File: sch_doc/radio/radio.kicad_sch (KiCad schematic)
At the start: 89 parts, among them IC1 MC34119, J1 tun, J2 out, J3 in_vol, J7 speaker, J8 vcc, J9 gnd, U1 ATTINY13A-PU, U2 TDA7088, U3 74HC595, U4 LM358

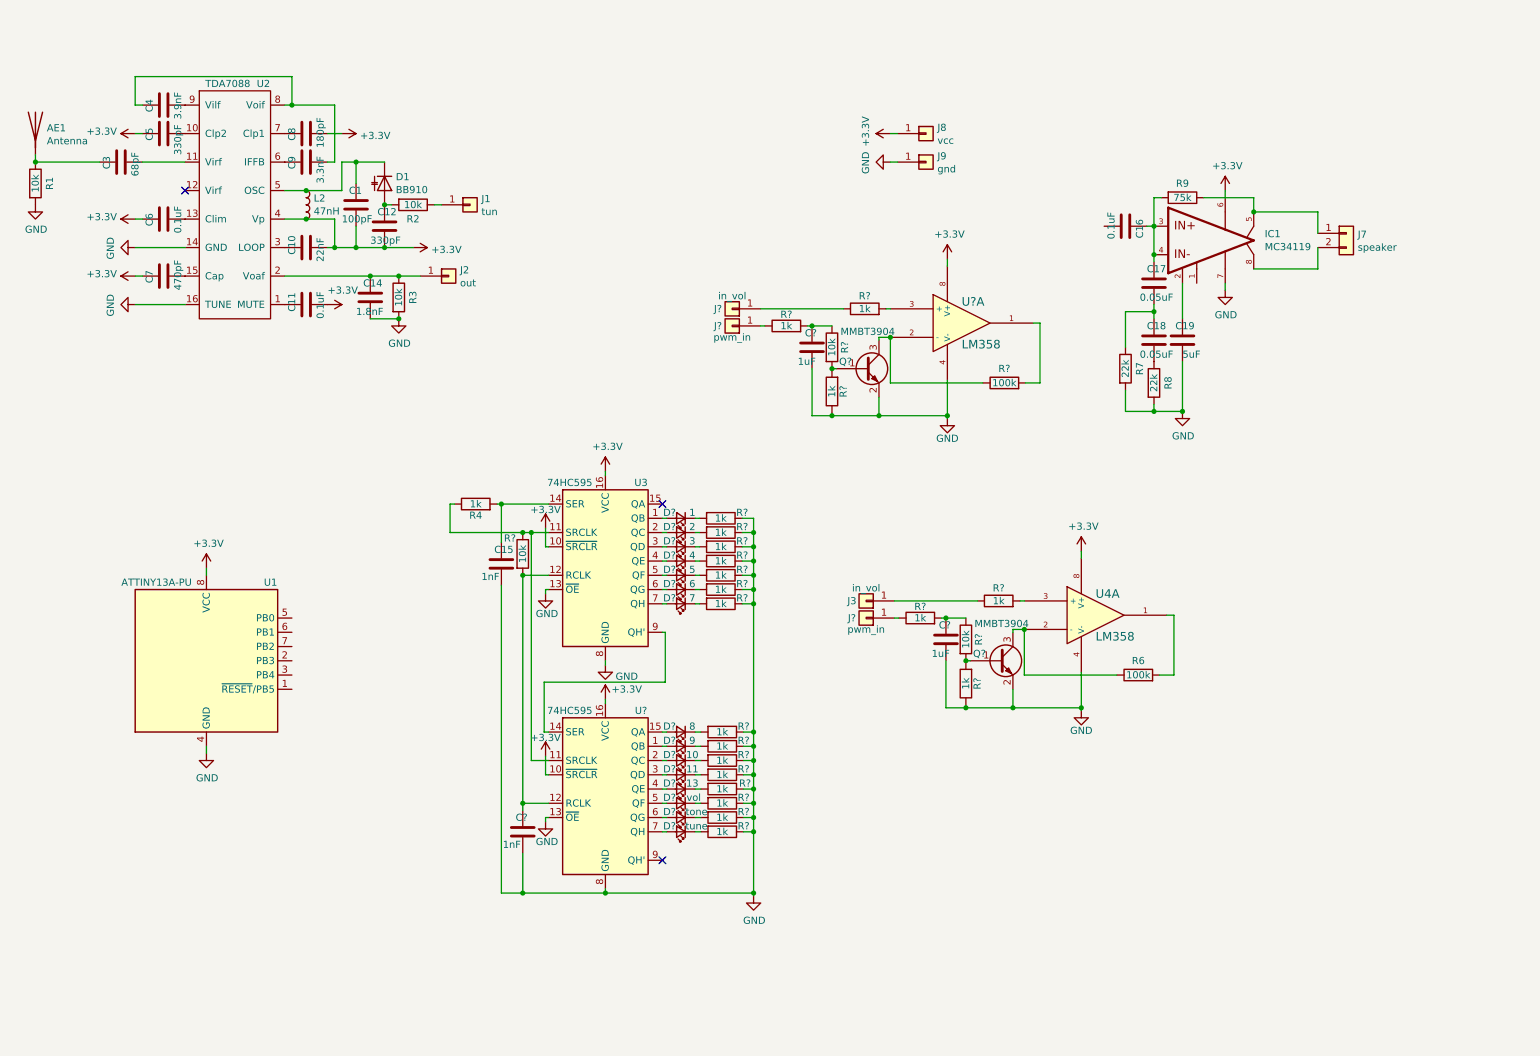
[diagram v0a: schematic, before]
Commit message: schematics ok, but not tested
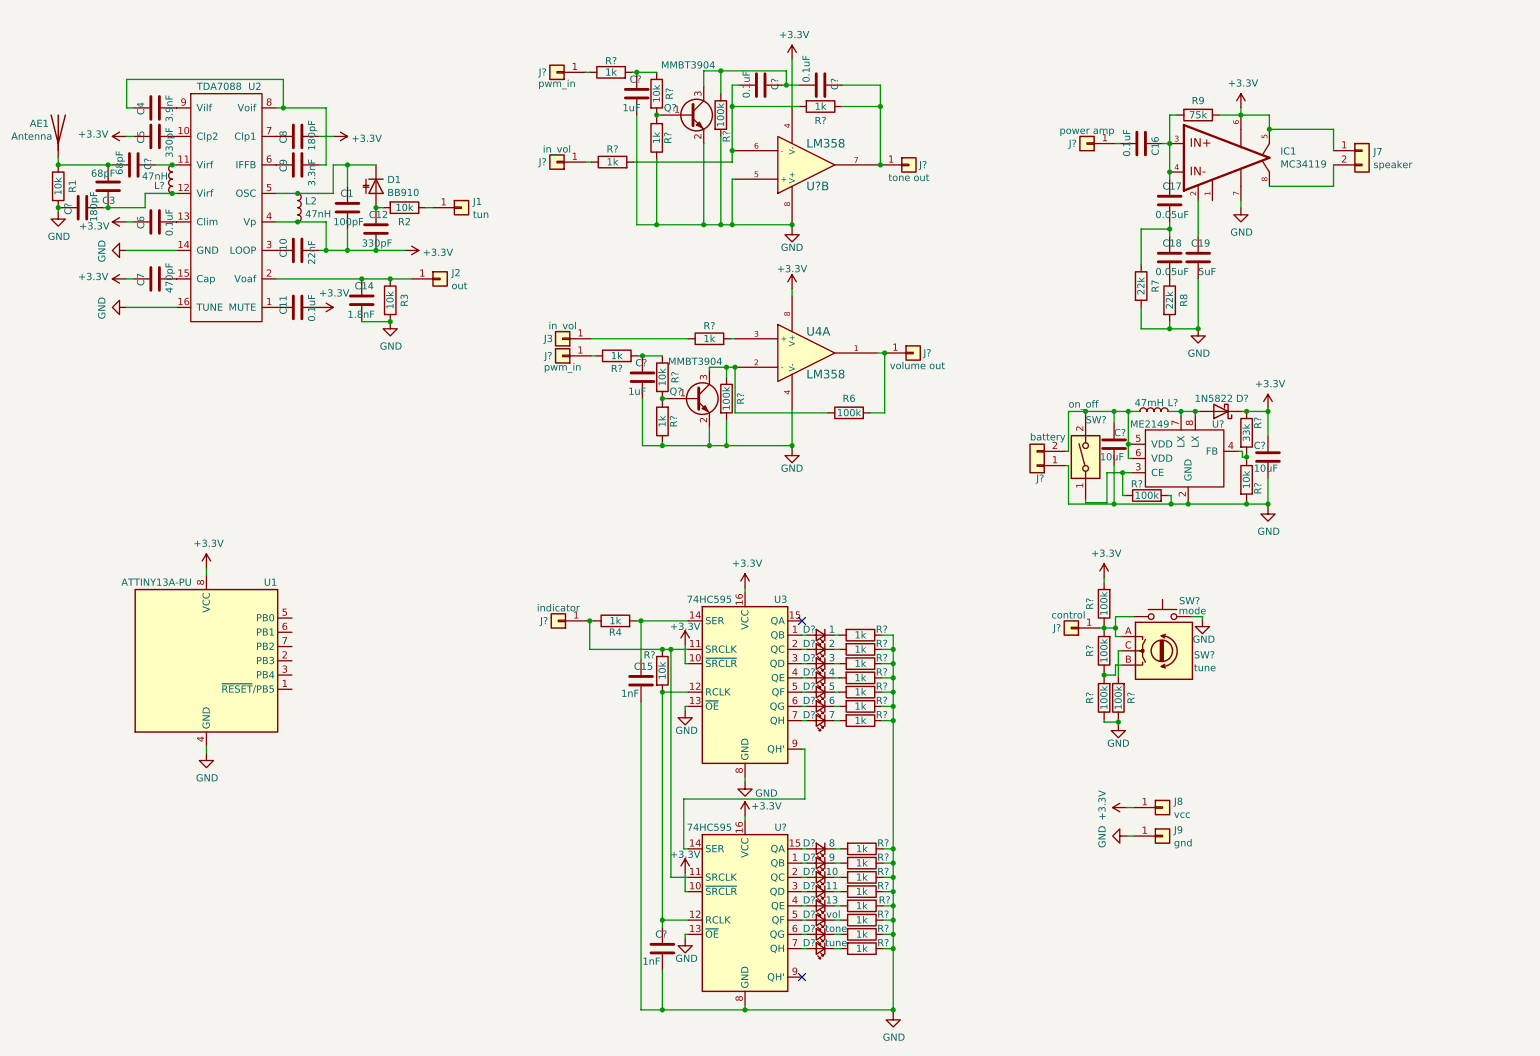
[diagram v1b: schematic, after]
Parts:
- removed C?: 1uF, Capacitor_SMD:C_0603_1608Metric, symbol Device:C
- removed Q?: MMBT3904, Package_TO_SOT_SMD:SOT-23, symbol Transistor_BJT:MMBT3904
- removed R? (x2): 1k, symbol Device:R
- removed R?: 10k, symbol Device:R
- added C?: 1uF, Capacitor_SMD:C_0603_1608Metric, symbol Device:C
- added C? (x2): 10uF, symbol Device:C
- added C? (x2): 0.1uF, symbol Device:C
- added C?: 68pF, Capacitor_SMD:C_0603_1608Metric, symbol Device:C
- added C?: 180pF, Capacitor_SMD:C_0603_1608Metric, symbol Device:C
- added D?: 1N5822, Diode_THT:D_DO-201AD_P15.24mm_Horizontal, symbol Diode:1N5822
- added J?: control, Connector_Wire:SolderWirePad_1x01_SMD_5x10mm, symbol Connector_Generic:Conn_01x01
- added J?: volume out, Connector_Wire:SolderWirePad_1x01_SMD_5x10mm, symbol Connector_Generic:Conn_01x01
- added J?: indicator, Connector_Wire:SolderWirePad_1x01_SMD_5x10mm, symbol Connector_Generic:Conn_01x01
- added J?: power amp, Connector_Wire:SolderWirePad_1x01_SMD_5x10mm, symbol Connector_Generic:Conn_01x01
- added J?: battery, symbol Connector_Generic:Conn_01x02
- added J?: tone out, Connector_Wire:SolderWirePad_1x01_SMD_5x10mm, symbol Connector_Generic:Conn_01x01
- added L?: 47mH, Inductor_SMD:L_0603_1608Metric_Pad1.05x0.95mm_HandSolder, symbol tda:L
- added L?: 47nH, Inductor_SMD:L_0603_1608Metric_Pad1.05x0.95mm_HandSolder, symbol tda:L
- added Q?: MMBT3904, Package_TO_SOT_SMD:SOT-23, symbol Transistor_BJT:MMBT3904
- added R? (x2): 1k, symbol Device:R
- added R? (x2): 10k, symbol Device:R
- added R?: 33k, symbol Device:R
- added R? (x6): 100k, Resistor_SMD:R_0805_2012Metric, symbol Device:R
- added R?: 100k, symbol Device:R
- added SW?: on_off, symbol Switch:SW_DIP_x01
- added SW?: mode, symbol Switch:SW_Push
- added SW?: tune, symbol Device:RotaryEncoder
- added U?: ME2149, symbol local:ME2149
- R?: value 100k -> 1k
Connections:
- net +3.3V: now also IC1.5, J7.1 (Pin_1), R9.1, U?.4 (V-), C?.2, D?.1 (K), R?.1, R?.2; no longer U?.8 (V+)
- net GND: now also U?.5 (+), U?.8 (V+), C?.1, C?.1, C?.1, C?.2, J?.1 (Pin_1), Q?.2 (E), R?.1, R?.1, R?.1, R?.2, R?.2, R?.2, R?.2, SW?.2, U?.2 (GND); no longer U?.4 (V-)
- net at C16.1: now also J?.1 (Pin_1)
- net at R4.1, R?.1, U3.11 (SRCLK)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: now also J?.1 (Pin_1)
- net at U2.11 (Virf): now also C?.2, L?.2; no longer C3.1
- net at U2.12 (Virf): now also C3.2, C?.1, L?.1
- net at R6.2, U4.1: now also J?.1 (Pin_1)
- net at Q?.3 (C), R6.1, U4.2 (-): now also R?.1
- net at AE1.1 (A), R1.1: now also C3.1, C?.1; no longer C3.2
- net at J?.1 (Pin_1): now also R?.1
- net at R?.2: now also R?.2, U?.6 (-), C?.1; no longer U?.1
- net at R?.1: now also U?.7, C?.2, J?.1 (Pin_1); no longer U?.2 (-)
- new net: C?.2, J?.2 (Pin_2), L?.1, SW?.2, U?.5 (VDD), U?.6 (VDD)
- new net: D?.2 (A), L?.2, U?.7 (LX), U?.8 (LX)
- new net: J?.1 (Pin_1), R?.1, R?.2, SW?.1, SW?.A
- new net: C?.2, R?.1, R?.2
- new net: Q?.1 (B), R?.2, R?.2
- new net: R?.1, SW?.1, U?.3 (CE)
- new net: C?.1, C?.2, Q?.3 (C), R?.1
- new net: R?.1, R?.2, SW?.B
- new net: R?.2, SW?.C
- new net: R?.1, R?.2, U?.4 (FB)
- no-connect marks 3 -> 2
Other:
- moved on the sheet: AE1, C1, C10, C11, C12, C14, C15, C16, C17, C18, C19, C3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

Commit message: pt2313 library element
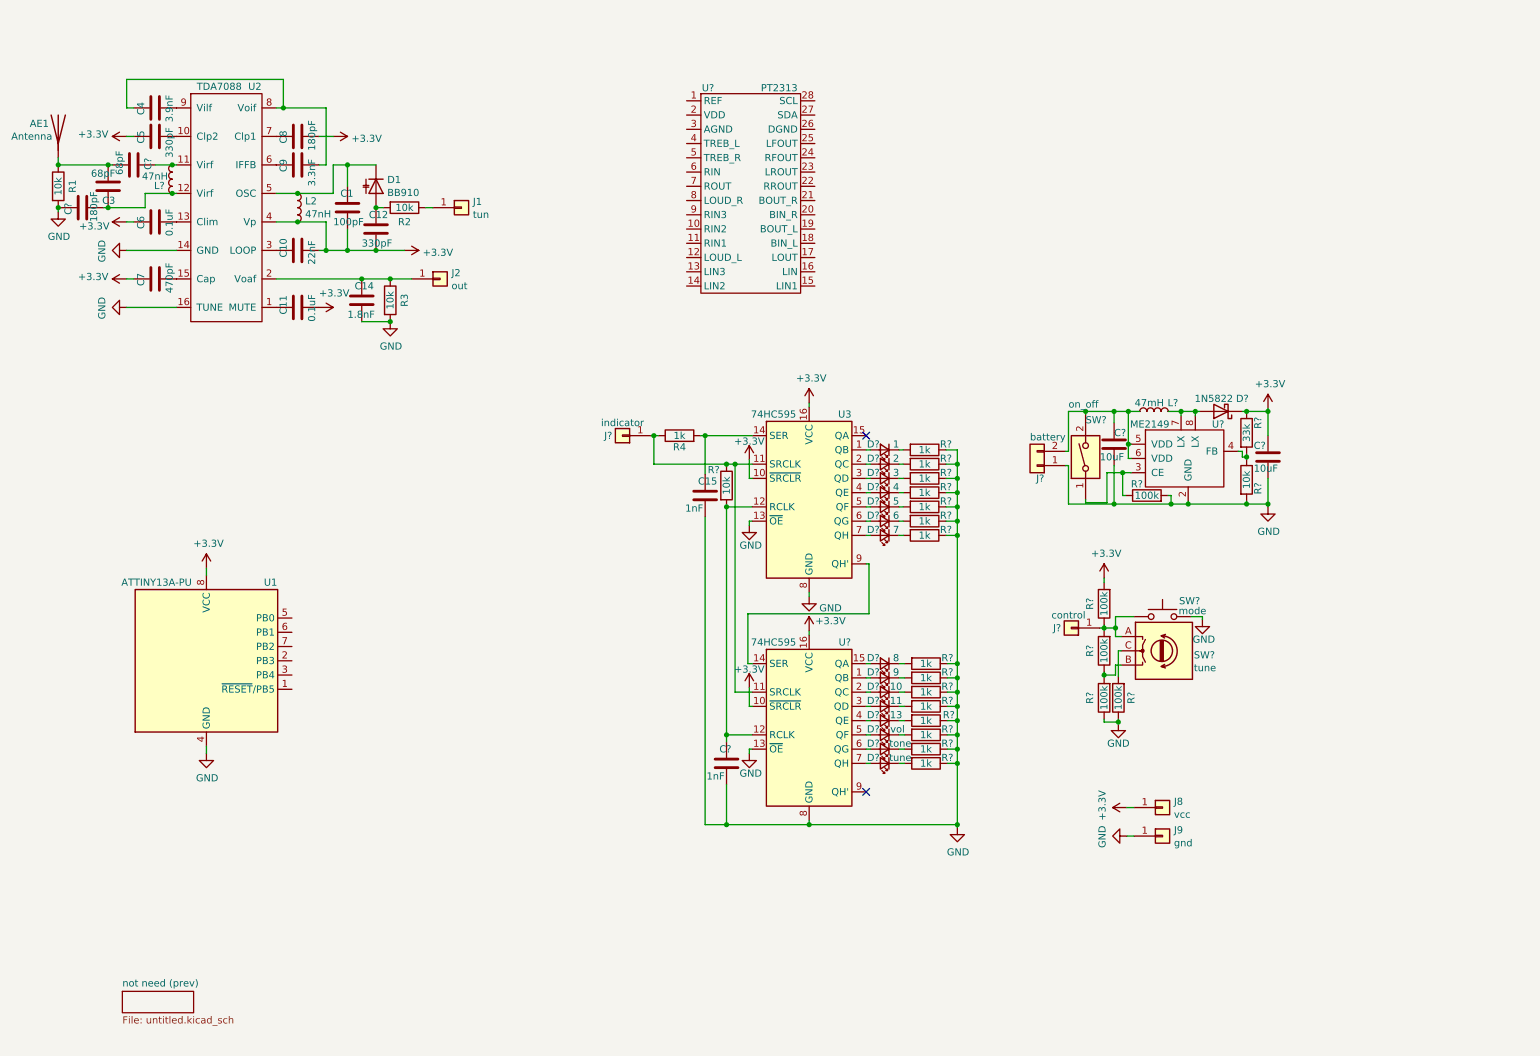
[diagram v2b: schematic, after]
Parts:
- removed C16, C? (x2): 0.1uF, symbol Device:C
- removed C17, C18: 0.05uF, symbol Device:C
- removed C19: 5uF, symbol Device:C
- removed C? (x2): 1uF, Capacitor_SMD:C_0603_1608Metric, symbol Device:C
- removed IC1: MC34119, symbol tda:MC34119
- removed J3, J?: in_vol, Connector_Wire:SolderWirePad_1x01_SMD_5x10mm, symbol Connector_Generic:Conn_01x01
- removed J7: speaker, symbol Connector_Generic:Conn_01x02
- removed J?: volume out, Connector_Wire:SolderWirePad_1x01_SMD_5x10mm, symbol Connector_Generic:Conn_01x01
- removed J? (x2): pwm_in, Connector_Wire:SolderWirePad_1x01_SMD_5x10mm, symbol Connector_Generic:Conn_01x01
- removed J?: power amp, Connector_Wire:SolderWirePad_1x01_SMD_5x10mm, symbol Connector_Generic:Conn_01x01
- removed J?: tone out, Connector_Wire:SolderWirePad_1x01_SMD_5x10mm, symbol Connector_Generic:Conn_01x01
- removed Q? (x2): MMBT3904, Package_TO_SOT_SMD:SOT-23, symbol Transistor_BJT:MMBT3904
- removed R6, R? (x2): 100k, Resistor_SMD:R_0805_2012Metric, symbol Device:R
- removed R7, R8: 22k, symbol Device:R
- removed R9: 75k, symbol Device:R
- removed R? (x6): 1k, symbol Device:R
- removed R? (x2): 10k, symbol Device:R
- removed R?: 1k, Resistor_SMD:R_0805_2012Metric, symbol Device:R
- removed U4, U?: LM358, Package_SO:SOP-8_3.9x4.9mm_P1.27mm, symbol tda:LM358
- added U?: PT2313, symbol local:PT2313
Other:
- added sheet not need (prev) (untitled.kicad_sch)
- moved on the sheet: C15, C?, D?, J?, R4, R?, U3, U?

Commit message: new schematics, I hope that it will be final
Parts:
- removed D?: tune, symbol Device:LED_Small
- removed D?: tone, symbol Device:LED_Small
- removed D?: vol, symbol Device:LED_Small
- removed J2: out, Connector_Wire:SolderWirePad_1x01_SMD_5x10mm, symbol Connector_Generic:Conn_01x01
- removed R?: 100k, symbol Device:R
- removed SW?: on_off, symbol Switch:SW_DIP_x01
- added C? (x3): 1uF, symbol Device:C
- added C? (x5): 0.1uF, Capacitor_SMD:C_0603_1608Metric, symbol Device:C
- added C? (x3): 100n, symbol Device:C
- added C?: 2.7n, symbol Device:C
- added C? (x3): 10uF, symbol Device:C
- added C?: 2.2n, symbol Device:C
- added D?: 14, symbol Device:LED_Small
- added J?: tune_enc, Connector_Wire:SolderWirePad_1x01_SMD_5x10mm, symbol Connector_Generic:Conn_01x01
- added J?: i2c, symbol Connector_Generic:Conn_01x02
- added J?: audio_ctl, symbol Connector_Generic:Conn_01x03
- added J?: pwr_on, Connector_Wire:SolderWirePad_1x01_SMD_5x10mm, symbol Connector_Generic:Conn_01x01
- added J?: control, symbol Connector_Generic:Conn_01x06
- added J?: speaker, symbol Connector_Generic:Conn_01x02
- added Q?: AO3401A, Package_TO_SOT_SMD:SOT-23, symbol Transistor_FET:AO3401A
- added R? (x4): 100k, Resistor_SMD:R_0805_2012Metric, symbol Device:R
- added R? (x4): 10k, symbol Device:R
- added SW?: tune, symbol Device:RotaryEncoder
- added SW?: auto/manual, symbol Switch:SW_Push
- added U?: LM4871, Package_SO:SOIC-8_3.9x4.9mm_P1.27mm, symbol local:LM4871
- J?: value control -> vol_enc
- SW?: value mode -> vol/tone
- SW?: value tune -> vol
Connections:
- net +3.3V: no longer C1.1, C10.1, C11.1, C12.1, C5.2, C6.2, C7.2, C8.1, C?.2, D?.1 (K), J8.1 (Pin_1), L2.2, R?.1, R?.2, U1.8 (VCC), U2.4 (Vp), U3.16 (VCC), U?.16 (VCC)
- net GND: now also U?.26 (DGND), U?.3 (AGND), C?.1, C?.1, C?.1, C?.1, C?.1, C?.1, C?.1, C?.1, C?.2, C?.2, C?.2, R?.1, R?.1, R?.2, SW?.2, U?.7 (V-); no longer R?.1, R?.1
- net at U1.1 (~{RESET}/PB5): now also J?.6 (Pin_6)
- net at U1.2 (PB3): now also J?.4 (Pin_4)
- net at U1.3 (PB4): now also J?.5 (Pin_5)
- net at U1.5 (PB0): now also J?.1 (Pin_1)
- net at U1.6 (PB1): now also J?.2 (Pin_2)
- net at U1.7 (PB2): now also J?.3 (Pin_3)
- net at C14.2, R3.1, U2.2 (Voaf): now also C?.2
- net at C?.2, J?.2 (Pin_2), L?.1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: now also U?.3 (CE)
- net at R?.2: now also U?.6 (QG)
- net at R?.2: now also U?.7 (QH)
- net at U?.1 (REF): now also C?.1
- net at U?.12 (LOUD_L): now also C?.1
- net at U?.14 (LIN2): now also C?.1
- net at U?.16 (LIN): now also C?.1
- net at U?.17 (LOUT): now also C?.2
- net at U?.18 (BIN_L): now also C?.1
- net at U?.19 (BOUT_L): now also C?.1
- net +5V: now reaches U?.2 (VDD)
- net +5V: now also C1.1, C10.1, C11.1, C12.1, C5.2, C6.2, C7.2, C8.1, L2.2, R?.2, U2.4 (Vp), U3.16 (VCC), U?.16 (VCC), C?.2, C?.2, C?.2, C?.2, C?.2, C?.2, Q?.3 (D), R?.2, U?.1 (SHUTDOWN), U?.6 (V+)
- net at U?.25 (LFOUT): now also C?.1
- net at U?.27 (SDA): now also J?.2 (Pin_2)
- net at U?.28 (SCL): now also J?.1 (Pin_1)
- net at U?.4 (TREB_L): now also C?.1
- net at U?.5 (QF): now also D?.2 (A)
- net at R?.2: now also D?.1 (K)
- new net: J?.1 (Pin_1), R?.1
- new net: J?.2 (Pin_2), R?.1
- new net: C?.2, U?.2 (BYPASS), U?.3 (IN+)
- new net: J?.1 (Pin_1), R?.1, R?.2, SW?.1, SW?.A
- new net: R?.1, R?.2, SW?.B
- new net: R?.2, SW?.C
- new net: R?.1, R?.2, U?.4 (IN-)
- new net: J?.1 (Pin_1), R?.2, U?.5 (VoutA)
- new net: C?.2, J?.3 (Pin_3), R?.1
- new net: J?.1 (Pin_1), Q?.1 (G), R?.2
- new net: J?.2 (Pin_2), U?.8 (VoutB)
- new net: C?.2, C?.2, R?.1
- new net +5VP: C?.2, C?.2, D?.1 (K), J8.1 (Pin_1), Q?.2 (S), R?.1, R?.1, U1.8 (VCC)
- no-connect marks 2 -> 16
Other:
- note added: "3W amplifier"
- note added: "MCU"
- note added: "led scale"
- note added: "step-up PWM"
- note added: "superheterodyne"
- note added: "tone filter"
- note added: "tune encoders"
- moved on the sheet: AE1, C1, C10, C11, C12, C14, C15, C3, C4, C5, C6, C7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
